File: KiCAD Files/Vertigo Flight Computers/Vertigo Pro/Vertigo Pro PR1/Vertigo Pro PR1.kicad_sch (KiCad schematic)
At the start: 142 parts, among them IC1 ICM-20602, IC2 DPS310XTSA1, IC3 MLX90393SLW-ABA-011-RE, J1 ST-LINK Conn, J2 USB_C_Receptacle_USB2.0, J3 FFC2A32-24-T, J4 Screw_Terminal, J5 Screw_Terminal, J6 Screw_Terminal, J7 Screw_Terminal, Q1 IRF530SPBF, Q2 IRF530SPBF, Q3 IRF530SPBF, Q4 IRF530SPBF, SW1 SW_SPDT, U1 STM32F103C8Tx, U10 TPS79133DBVR, U11 TLV709, U12 TLV709, U13 TLV75528PDBV, U2 AP63203WU, U3 ESP32-S3-WROOM-1, U4 TLV75515PDBV, U6 W25Q64FV, U7 TPS2121RUXR, U8 NEO-6M-GPS, U9 24AA32A-I_MS, Y1 16MHz

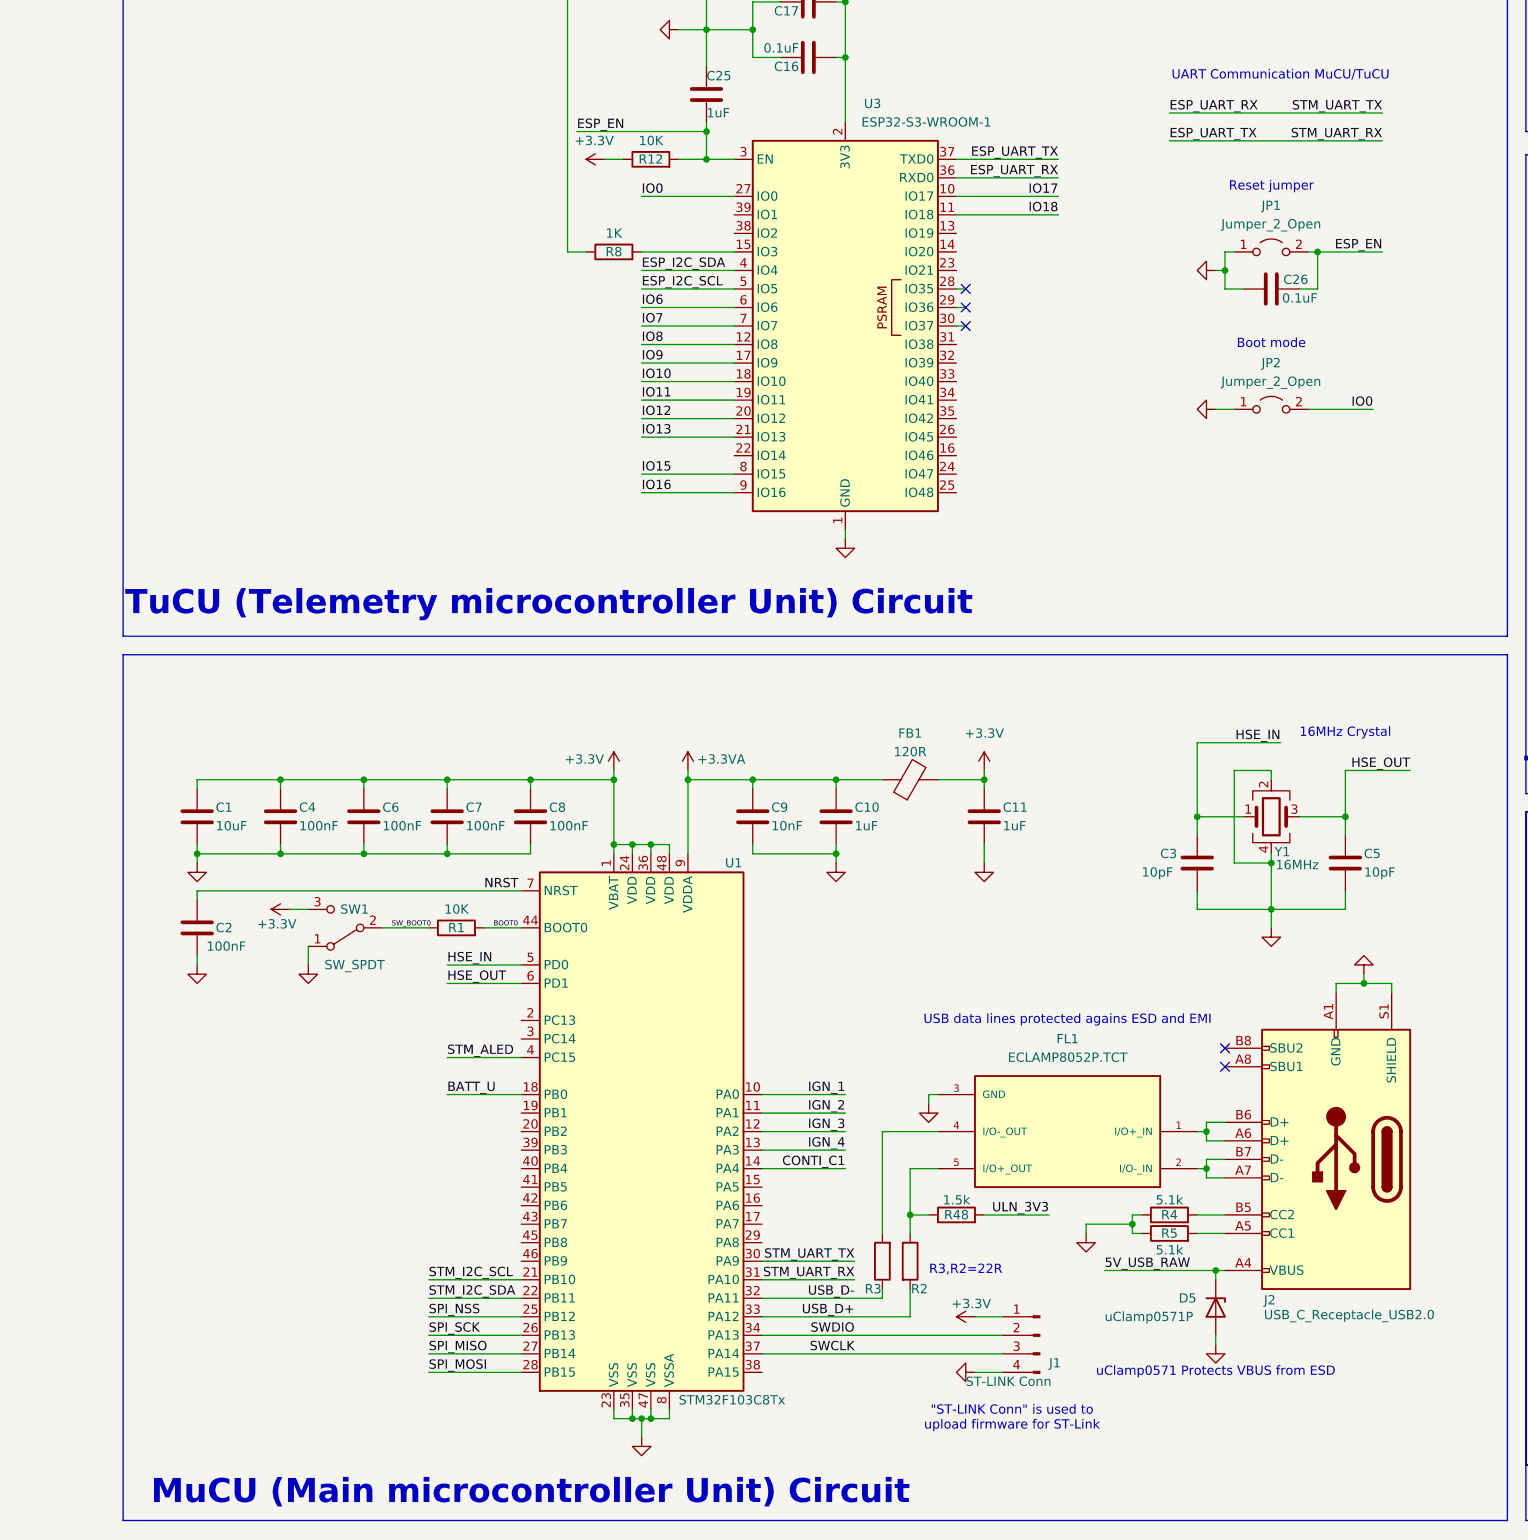
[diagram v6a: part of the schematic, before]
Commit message: Bootloader mode selection
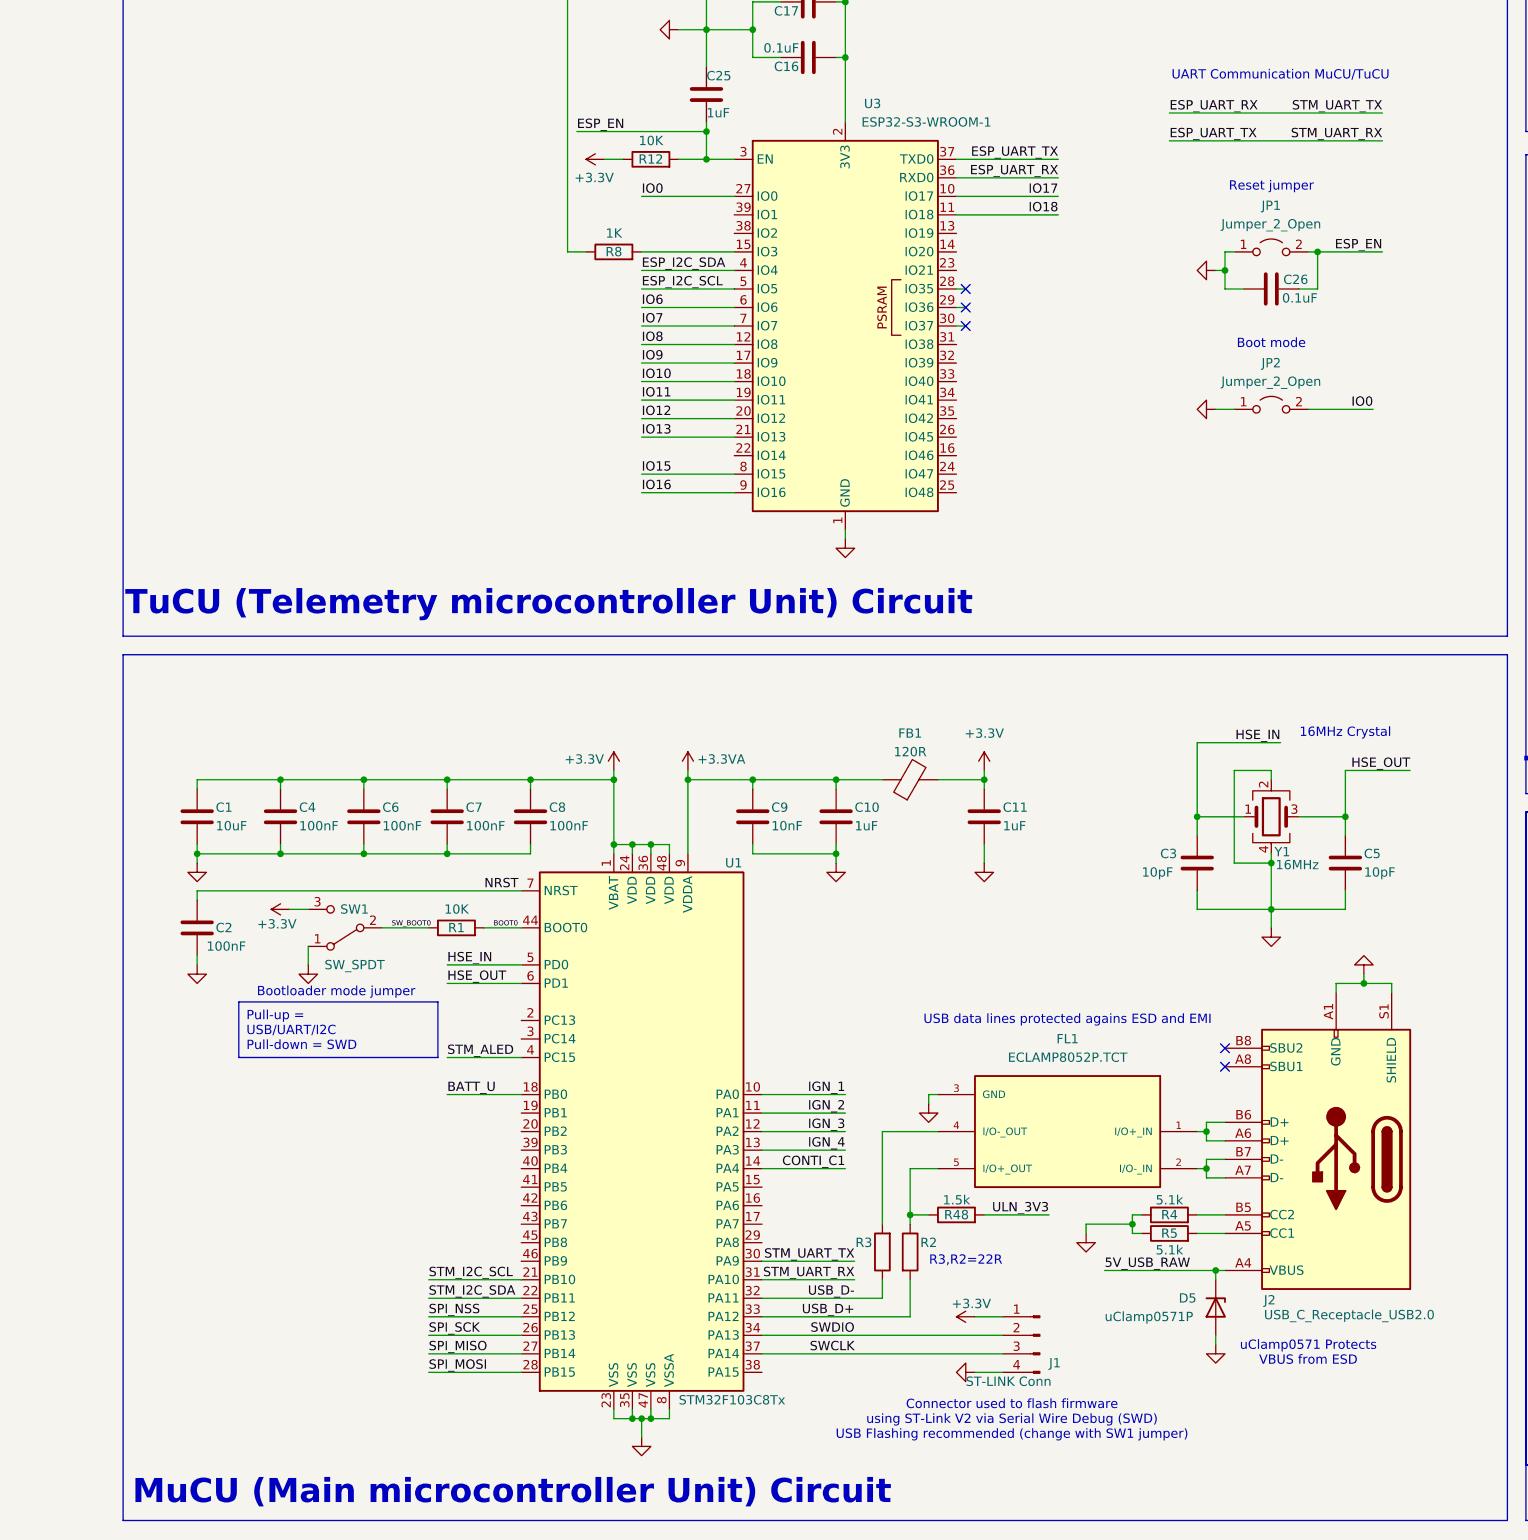
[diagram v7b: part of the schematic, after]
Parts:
- SW1: footprint (none) -> Jumper:SolderJumper-3_P2.0mm_Open_TrianglePad1.0x1.5mm_NumberLabels
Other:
- note added: "Bootloader mode jumper"
- note added: "Connector used to flash firmware using ST-Link V2 via Serial Wire Debug (SWD) USB Flashing recommended (change with SW1 jumper)"
- note removed: ""ST-LINK Conn" is used to upload firmware for ST-Link"
- moved on the sheet: R2, R3
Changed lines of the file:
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@@
 	(wire
 		(pts
-			(xy 118.11 322.58) (xy 118.11 323.85)
+			(xy 118.11 321.31) (xy 118.11 323.85)
 		)
 		(stroke
@@
 	(wire
 		(pts
-			(xy 118.11 314.96) (xy 118.11 300.99)
+			(xy 118.11 313.69) (xy 118.11 300.99)
 		)
 		(stroke
@@
 	(wire
 		(pts
-			(xy 121.92 312.42) (xy 121.92 314.96)
-		)
-		(stroke
-			(width 0)
-			(type default)
-		)
-	)
-	(wire
-		(pts
 			(xy 93.98 149.86) (xy 100.33 149.86)
 		)
@@
 	(wire
 		(pts
+			(xy 121.92 313.69) (xy 121.92 312.42)
+		)
+		(stroke
+			(width 0)
+			(type default)
+		)
+	)
+	(wire
+		(pts
 			(xy 519.43 132.08) (xy 519.43 130.81)
 		)
@@
 	(wire
 		(pts
-			(xy 121.92 326.39) (xy 121.92 322.58)
+			(xy 121.92 326.39) (xy 121.92 321.31)
 		)
 		(stroke
@@
 		)
 	)
+	(text_box "Pull-up = USB/UART/I2C\nPull-down = SWD"
+		(exclude_from_sim no)
+		(at 29.845 283.21 0)
+		(size 27.305 7.62)
+		(stroke
+			(width 0)
+			(type default)
+		)
+		(fill
+			(type none)
+		)
+		(effects
+			(font
+				(size 1.27 1.27)
+			)
+			(justify left top)
+		)
+	)
 	(text_box "check SPI connections to stm!!!"
 		(exclude_from_sim no)
@@
 		)
 	)
-	(text "\"ST-LINK Conn\" is used to \nupload firmware for ST-Link"
+	(text "Connector used to flash firmware \nusing ST-Link V2 via Serial Wire Debug (SWD)\nUSB Flashing recommended (change with SW1 jumper)\n\n"
 		(exclude_from_sim no)
-		(at 135.89 340.36 0)
+		(at 135.89 341.63 0)
 		(effects
 			(font
@@
 	(text "MuCU (Main microcontroller Unit) Circuit"
 		(exclude_from_sim no)
-		(at 69.85 350.52 0)
+		(at 67.31 350.52 0)
 		(effects
 			(font
@@
 		)
 	)
-	(text "uClamp0571 Protects VBUS from ESD"
+	(text "uClamp0571 Protects \nVBUS from ESD"
 		(exclude_from_sim no)
-		(at 163.83 334.01 0)
+		(at 176.53 331.47 0)
 		(effects
 			(font
@@
 		)
 	)
+	(text "Bootloader mode jumper\n"
+		(exclude_from_sim no)
+		(at 43.18 281.94 0)
+		(effects
+			(font
+				(size 1.27 1.27)
+			)
+		)
+	)
 	(text "Channel 4\n"
 		(exclude_from_sim no)
@@
 	(text "R3,R2=22R"
 		(exclude_from_sim no)
-		(at 129.54 320.04 0)
+		(at 129.54 318.77 0)
 		(effects
 			(font
@@
 		)
 		(property "Value" "+3.3V"
-			(at 81.28 165.1 90)
+			(at 81.28 170.18 90)
 			(effects
 				(font
@@
 			)
 		)
-		(property "Footprint" ""
+		(property "Footprint" "Jumper:SolderJumper-3_P2.0mm_Open_TrianglePad1.0x1.5mm_NumberLabels"
 			(at 44.45 273.05 0)
 			(effects
@@
 	(symbol
 		(lib_id "Device:R")
-		(at 121.92 318.77 0)
+		(at 121.92 317.5 0)
 		(unit 1)
 		(exclude_from_sim no)
@@
 		(dnp no)
 		(property "Reference" "R2"
-			(at 123.19 322.58 0)
+			(at 124.46 316.23 0)
 			(effects
 				(font
@@
 		)
 		(property "Value" "22R"
-			(at 125.73 317.5 0)
+			(at 125.73 316.23 0)
 			(effects
 				(font
@@
 		)
 		(property "Footprint" "Resistor_SMD:R_0603_1608Metric"
-			(at 120.142 318.77 90)
+			(at 120.142 317.5 90)
 			(effects
 				(font
@@
 		)
 		(property "Datasheet" "~"
-			(at 121.92 318.77 0)
+			(at 121.92 317.5 0)
 			(effects
 				(font
@@
 		)
 		(property "Description" "Resistor"
-			(at 121.92 318.77 0)
+			(at 121.92 317.5 0)
 			(effects
 				(font
@@
 	(symbol
 		(lib_id "Device:R")
-		(at 118.11 318.77 180)
+		(at 118.11 317.5 180)
 		(unit 1)
 		(exclude_from_sim no)
@@
 		(dnp no)
 		(property "Reference" "R3"
-			(at 116.84 322.58 0)
+			(at 115.57 316.23 0)
 			(effects
 				(font
@@
 		)
 		(property "Value" "22R"
-			(at 125.73 323.85 0)
+			(at 125.73 322.58 0)
 			(effects
 				(font
@@
 		)
 		(property "Footprint" "Resistor_SMD:R_0603_1608Metric"
-			(at 119.888 318.77 90)
+			(at 119.888 317.5 90)
 			(effects
 				(font
@@
 		)
 		(property "Datasheet" "~"
-			(at 118.11 318.77 0)
+			(at 118.11 317.5 0)
 			(effects
 				(font
@@
 		)
 		(property "Description" "Resistor"
-			(at 118.11 318.77 0)
+			(at 118.11 317.5 0)
 			(effects
 				(font

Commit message: Annotations, footprints etc.
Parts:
- C49, C50: footprint (none) -> Resistor_SMD:R_0402_1005Metric_Pad0.72x0.64mm_HandSolder
- L1: footprint (none) -> Vertigo Pro KiCad Libraries:CDMC6D28NP-4R7MC
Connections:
- net STM_I2C_SCL is gone; now on net ESP_I2C_SCL: IC1.2 (SCL/SPC), IC2.4 (SCK), IC3.3 (SCL/SCLK), R29.1, U1.21 (PB10), U8.19 (SCL2), U9.6 (SCL)
- net STM_I2C_SDA is gone; now on net DVP_VSYNC: IC1.3 (SDA/SDI), IC2.3 (SDI), IC3.5 (SDA/MOSI), R30.1, U1.22 (PB11), U8.18 (SDA2), U9.5 (SDA)
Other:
- note added: "I2C Communication"
- note added: "MuCU/TuCU Communication"
- note added: "UART Communication"
- note removed: "UART Communication MuCU/TuCU"
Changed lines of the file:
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@@
 	(wire
 		(pts
-			(xy 157.48 161.29) (xy 186.69 161.29)
+			(xy 210.82 99.06) (xy 240.03 99.06)
 		)
 		(stroke
@@
 	(wire
 		(pts
+			(xy 245.11 102.87) (xy 273.05 102.87)
+		)
+		(stroke
+			(width 0)
+			(type default)
+		)
+	)
+	(wire
+		(pts
 			(xy 278.13 213.36) (xy 297.18 213.36)
 		)
@@
 	(wire
 		(pts
-			(xy 157.48 165.1) (xy 186.69 165.1)
+			(xy 210.82 102.87) (xy 240.03 102.87)
 		)
 		(stroke
@@
 	(wire
 		(pts
+			(xy 245.11 99.06) (xy 273.05 99.06)
+		)
+		(stroke
+			(width 0)
+			(type default)
+		)
+	)
+	(wire
+		(pts
 			(xy 180.34 280.67) (xy 184.15 280.67)
 		)
@@
 	)
 	(rectangle
-		(start 136.525 63.5)
+		(start 135.89 63.5)
 		(end 172.085 125.73)
 		(stroke
@@
 	)
 	(rectangle
+		(start 206.375 83.82)
+		(end 278.13 117.475)
+		(stroke
+			(width 0)
+			(type default)
+		)
+		(fill
+			(type none)
+		)
+	)
+	(rectangle
 		(start 476.885 97.155)
 		(end 582.295 179.705)
@@
 		)
 	)
+	(text "MuCU/TuCU Communication"
+		(exclude_from_sim no)
+		(at 242.57 114.3 0)
+		(effects
+			(font
+				(size 3.302 3.302)
+				(bold yes)
+			)
+		)
+	)
 	(text "Pyrotechnical Channels"
 		(exclude_from_sim no)
@@
 		)
 	)
+	(text "I2C Communication"
+		(exclude_from_sim no)
+		(at 259.08 95.25 0)
+		(effects
+			(font
+				(size 1.27 1.27)
+			)
+		)
+	)
 	(text "Inerial Measurement Unit (IMU)"
 		(exclude_from_sim no)
@@
 		)
 	)
-	(text "UART Communication MuCU/TuCU"
+	(text "UART Communication\n"
 		(exclude_from_sim no)
-		(at 172.72 156.21 0)
+		(at 226.06 95.25 0)
 		(effects
 			(font
@@
 		)
 	)
+	(label "ESP_I2C_SDA"
+		(at 273.05 102.87 180)
+		(fields_autoplaced yes)
+		(effects
+			(font
+				(size 1.27 1.27)
+			)
+			(justify right bottom)
+		)
+	)
 	(label "IO16"
 		(at 85.09 213.36 0)
@@
 	)
 	(label "STM_UART_RX"
-		(at 186.69 165.1 180)
+		(at 240.03 102.87 180)
 		(fields_autoplaced yes)
 		(effects
@@
 	)
 	(label "ESP_UART_TX"
-		(at 157.48 165.1 0)
+		(at 210.82 102.87 0)
 		(fields_autoplaced yes)
 		(effects
@@
 		)
 	)
+	(label "ESP_I2C_SCL"
+		(at 273.05 99.06 180)
+		(fields_autoplaced yes)
+		(effects
+			(font
+				(size 1.27 1.27)
+			)
+			(justify right bottom)
+		)
+	)
 	(label "IGN_3"
 		(at 78.74 60.96 0)
@@
 	)
 	(label "STM_UART_TX"
-		(at 186.69 161.29 180)
+		(at 240.03 99.06 180)
 		(fields_autoplaced yes)
 		(effects
@@
 		)
 	)
+	(label "STM_I2C_SCL"
+		(at 245.11 99.06 0)
+		(fields_autoplaced yes)
+		(effects
+			(font
+				(size 1.27 1.27)
+			)
+			(justify left bottom)
+		)
+	)
 	(label "ESP_UART_RX"
-		(at 157.48 161.29 0)
+		(at 210.82 99.06 0)
 		(fields_autoplaced yes)
 		(effects
@@
 		)
 	)
+	(label "STM_I2C_SDA"
+		(at 245.11 102.87 0)
+		(fields_autoplaced yes)
+		(effects
+			(font
+				(size 1.27 1.27)
+			)
+			(justify left bottom)
+		)
+	)
 	(label "I2C_SDA"
 		(at 297.18 186.69 180)
@@
 			)
 		)
-		(property "Footprint" ""
+		(property "Footprint" "Vertigo Pro KiCad Libraries:CDMC6D28NP-4R7MC"
 			(at 543.56 288.29 0)
 			(effects
@@
 			)
 		)
-		(property "Footprint" ""
+		(property "Footprint" "Resistor_SMD:R_0402_1005Metric_Pad0.72x0.64mm_HandSolder"
 			(at 278.4348 125.73 0)
 			(effects
@@
 	(symbol
 		(lib_id "proxima_logo:LOGO")
-		(at 285.75 46.99 0)
+		(at 283.21 -33.02 0)
 		(unit 1)
 		(exclude_from_sim no)
@@
 		(fields_autoplaced yes)
 		(property "Reference" "#G1"
-			(at 285.75 26.8123 0)
+			(at 283.21 -53.1977 0)
 			(effects
 				(font
@@
 		)
 		(property "Value" "LOGO"
-			(at 285.75 67.1677 0)
+			(at 283.21 -12.8423 0)
 			(effects
 				(font
@@
 		)
 		(property "Footprint" ""
-			(at 285.75 46.99 0)
+			(at 283.21 -33.02 0)
 			(effects
 				(font
@@
 		)
 		(property "Datasheet" ""
-			(at 285.75 46.99 0)
+			(at 283.21 -33.02 0)
 			(effects
 				(font
@@
 		)
 		(property "Description" ""
-			(at 285.75 46.99 0)
+			(at 283.21 -33.02 0)
 			(effects
 				(font
@@
 			)
 		)
-		(property "Footprint" ""
+		(property "Footprint" "Resistor_SMD:R_0402_1005Metric_Pad0.72x0.64mm_HandSolder"
 			(at 235.2548 125.73 0)
 			(effects
